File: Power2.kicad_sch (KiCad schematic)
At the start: 23 parts, among them U14 Opamp_Quad, U5 IRS2186, U6 IRS2186, U7 IRS2186

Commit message: - layout almost finished
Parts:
- removed C3: 1u, Capacitor_SMD:C_0805_2012Metric, symbol Device:C
- added U14: Opamp_Quad, Package_SO:SO-14_3.9x8.65mm_P1.27mm, symbol Device:Opamp_Quad
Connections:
- net GND: now also U14.10 (+)
- net U_GH renamed U2_GH
- net U_GL renamed U2_GL
- net U_PWM_H renamed U2_PWM_H
- net U_PWM_L renamed U2_PWM_L
- net U_U renamed U2_U
- net U_VP renamed U2_VP
- net V_GH renamed V2_GH
- net V_GL renamed V2_GL
- net V_PWM_H renamed V2_PWM_H
- net V_PWM_L renamed V2_PWM_L
- net V_U renamed V2_U
- net V_VP renamed V2_VP
- net W_GH renamed W2_GH
- net W_GL renamed W2_GL
- net W_PWM_H renamed W2_PWM_H
- net W_PWM_L renamed W2_PWM_L
- net W_U renamed W2_U
- net W_VP renamed W2_VP
- new net: U14.8, U14.9 (-)
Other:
- moved on the sheet: U14E

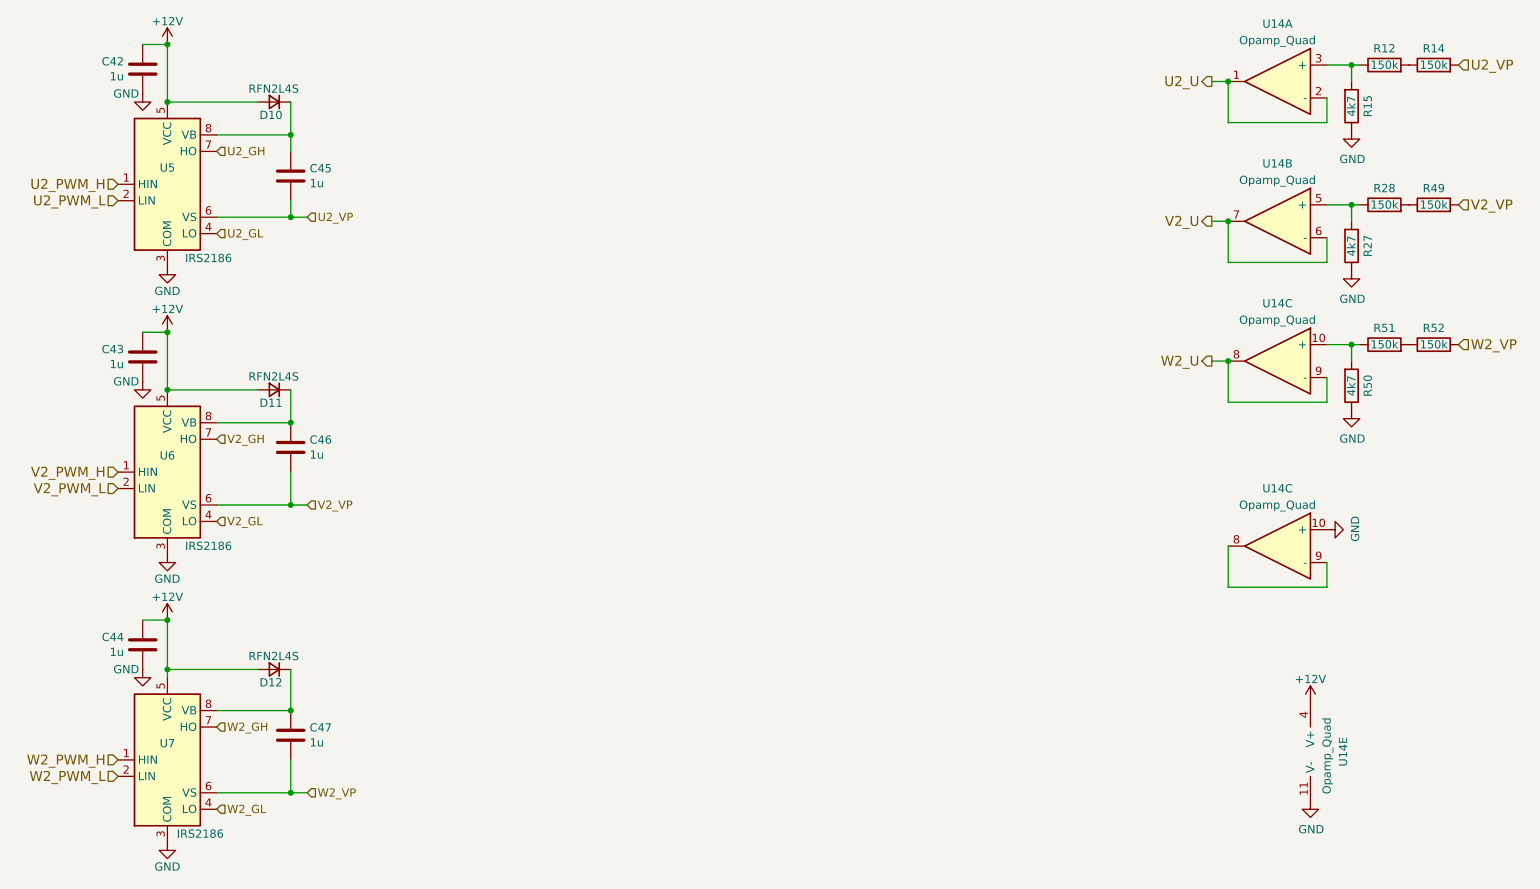
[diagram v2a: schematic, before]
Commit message: - fixed missing 3V3 trace on USB isolator
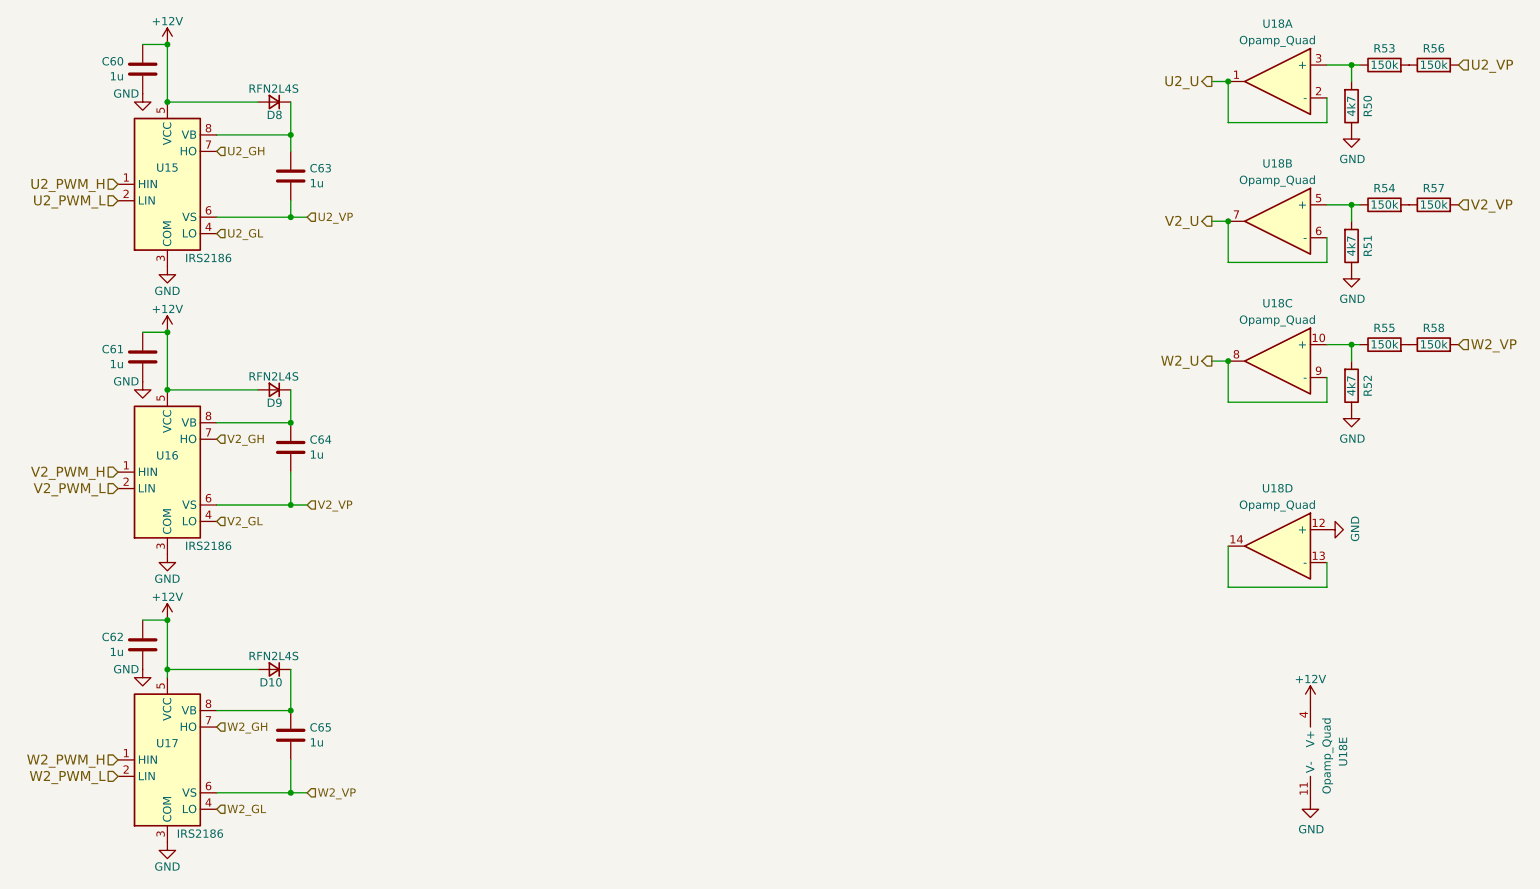
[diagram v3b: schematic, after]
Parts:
- renumbered C42 to C60, C43 to C61, C44 to C62, C45 to C63, C46 to C64, C47 to C65, D12 to D10, D10 to D8, D11 to D9, R15 to R50, R27 to R51, R50 to R52, R12 to R53, R28 to R54, R51 to R55, R14 to R56, R49 to R57, R52 to R58, U5 to U15, U6 to U16, U7 to U17, U14 to U18
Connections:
- net GND: now also U18.12 (+); no longer U18.10 (+)
- new net: U18.13 (-), U18.14
